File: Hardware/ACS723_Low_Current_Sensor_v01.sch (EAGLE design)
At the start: 26 parts, among them U1 ACS723, U2 OPA344

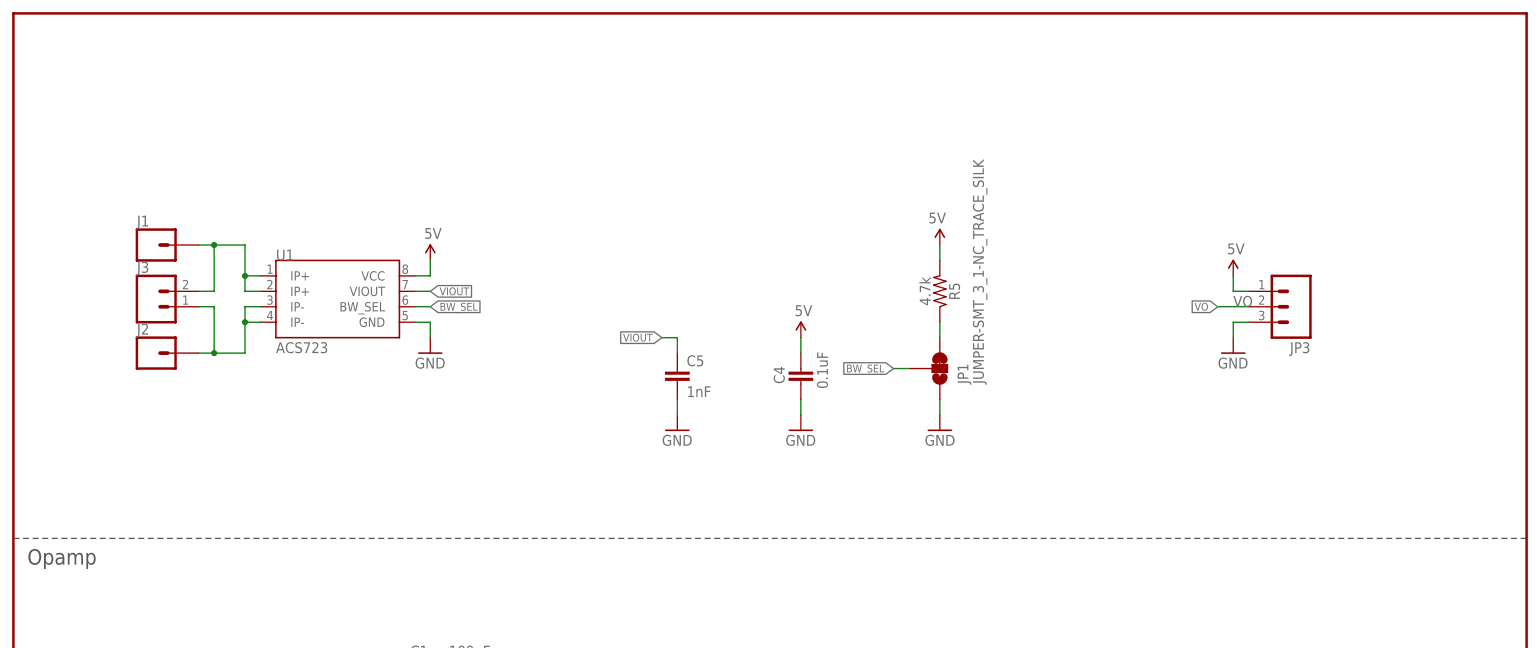
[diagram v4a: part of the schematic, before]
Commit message: v01 checklist issues
-added voltage and current ranges
-labeled JP1 in the SCH
-reorganized the SCH
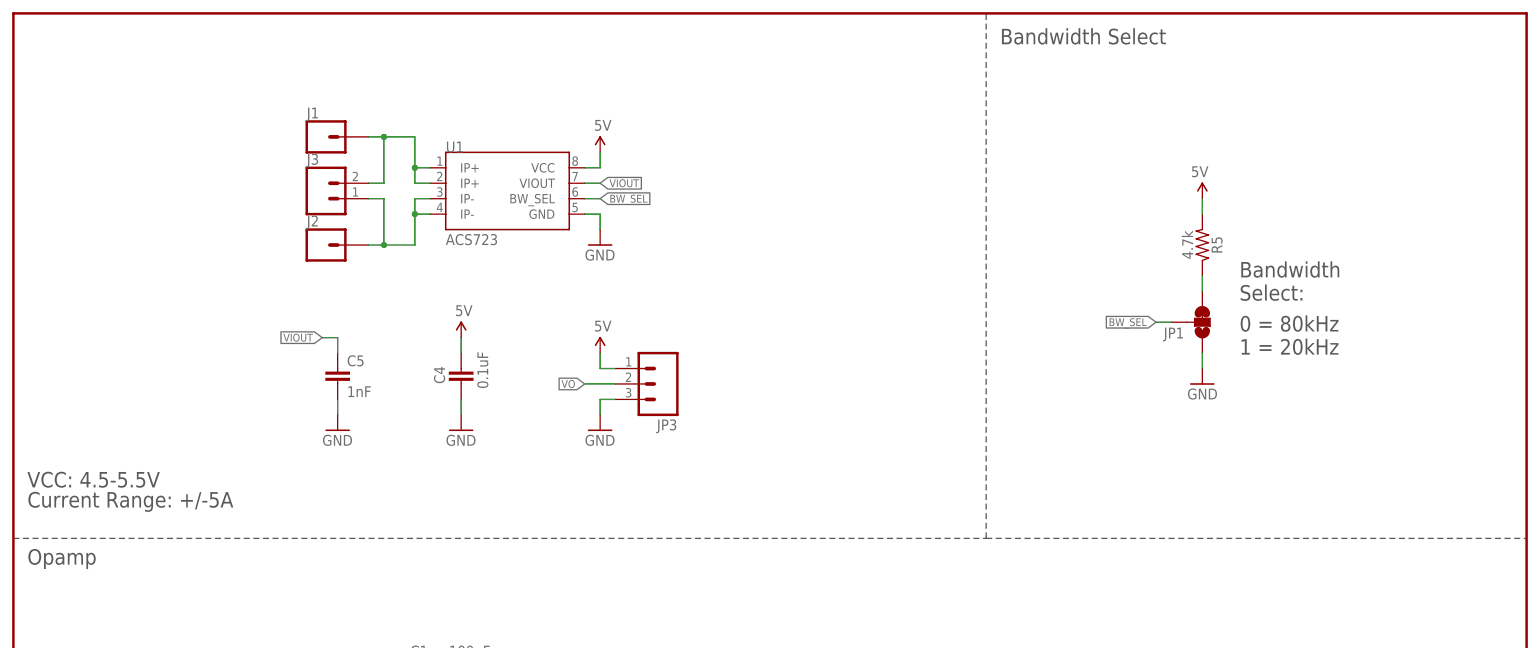
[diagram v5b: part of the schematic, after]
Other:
- note added: "0 = 80kHz"
- note added: "1 = 20kHz"
- note added: "Bandwidth Select"
- note added: "Bandwidth Select:"
- note added: "Current Range: +/-5A"
- note added: "VCC: 4.5-5.5V"
- moved on the sheet: C4, C5, J1, J2, J3, JP1, JP3, R5, U1
